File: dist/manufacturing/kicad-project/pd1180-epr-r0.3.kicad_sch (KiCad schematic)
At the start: 0 parts

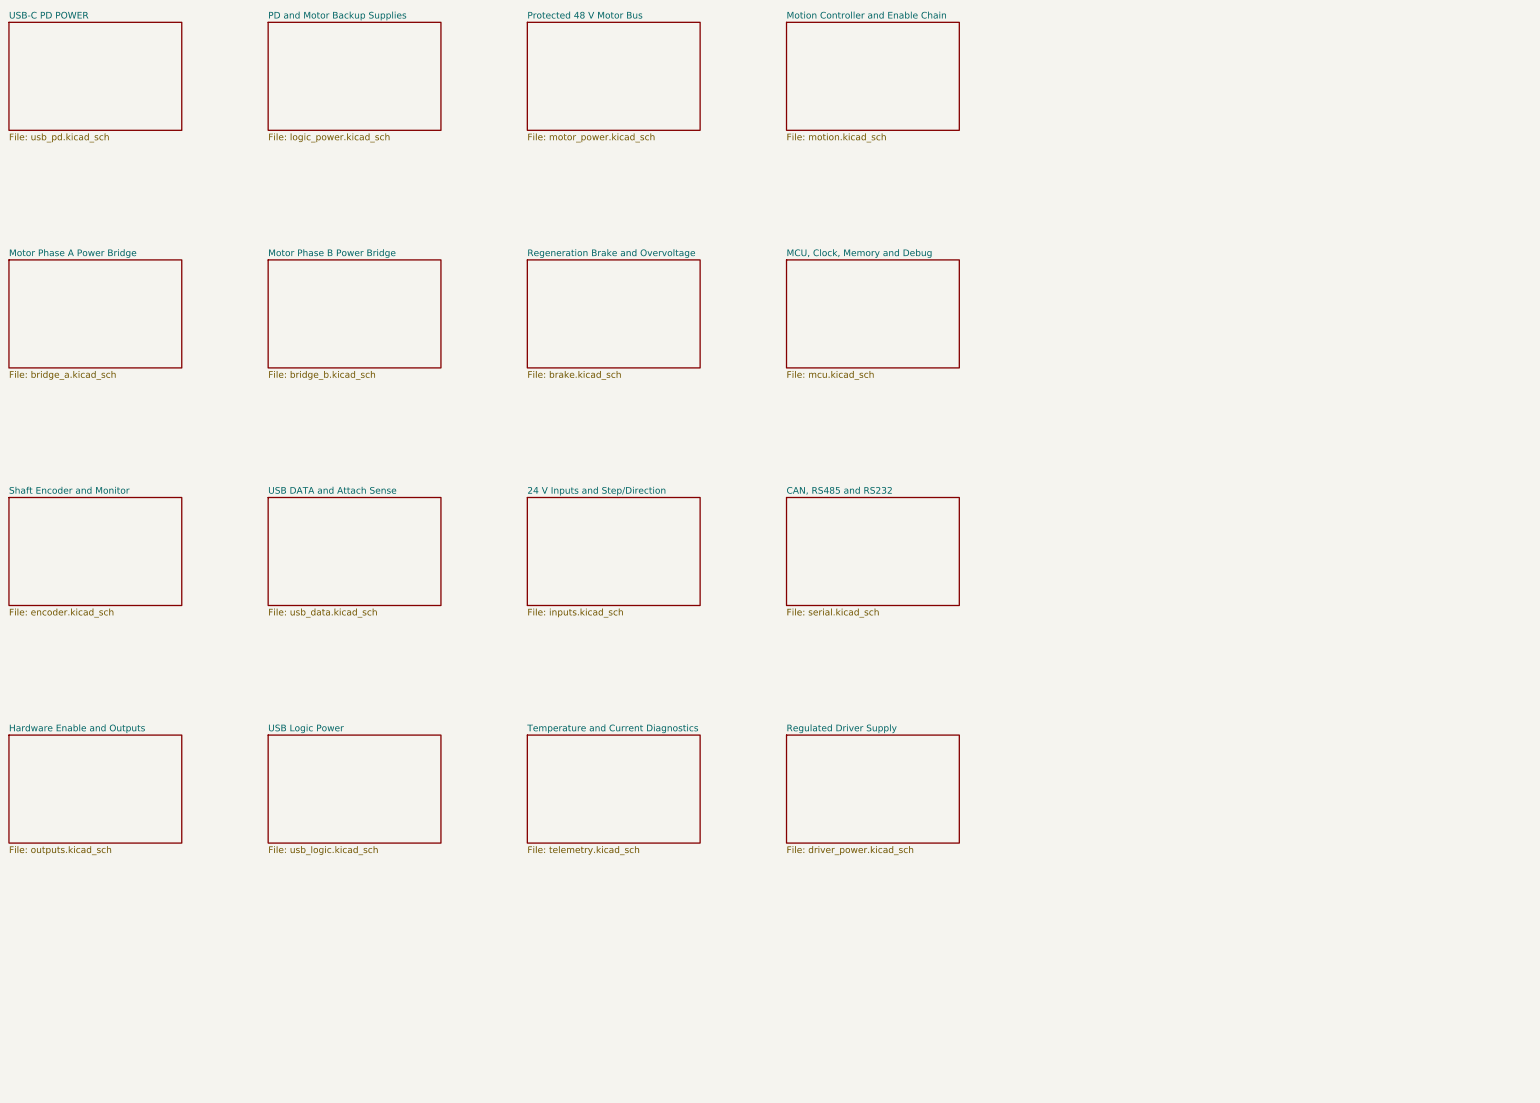
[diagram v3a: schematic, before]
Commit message: Add routed diagnostics and isolated PD programming access
Add RGB and independent power indication, a reset-safe driven buzzer,
isolated EEPROM programming access, and eight power/programming probes.
Preserve top-side assembly and local bypass paths, and exclude all bare
service contacts from stencil paste.

Refresh firmware, Gerbers, BOM/CPL, 3D models and review documentation.
The full review passes 32 checks and 55 regression tests, with zero native
DRC, ERC, unconnected and schematic-parity issues. TI configuration and
physical qualification remain explicit order holds.
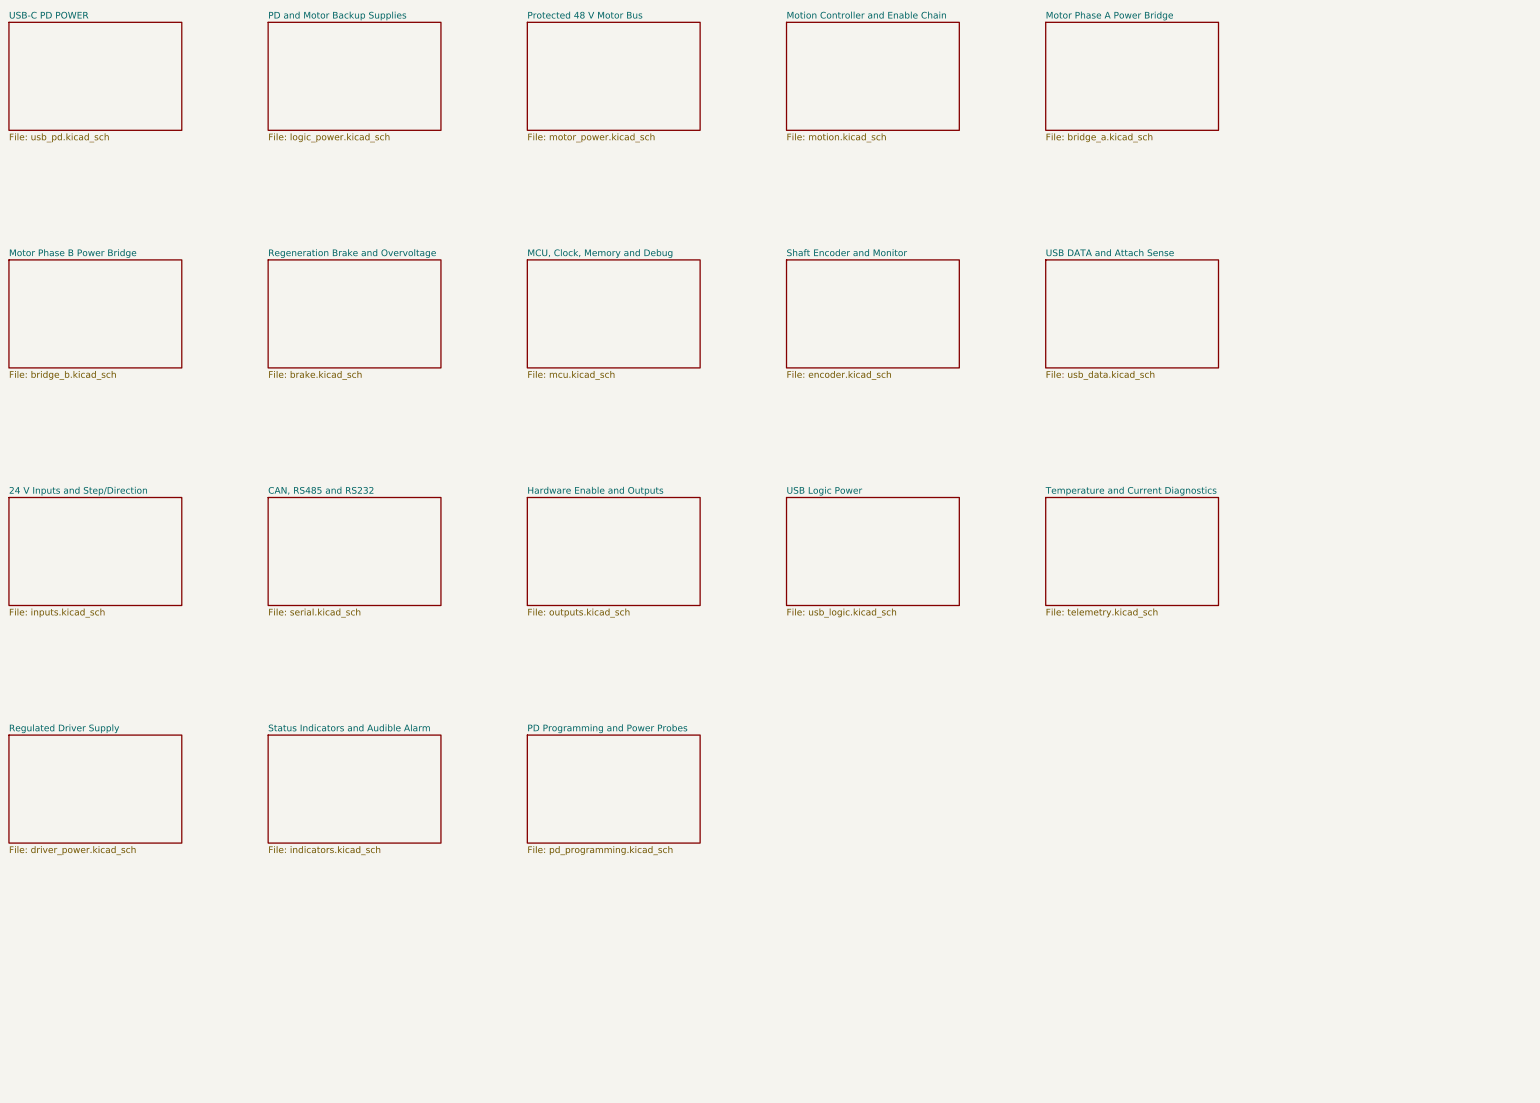
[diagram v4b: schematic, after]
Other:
- added sheet PD Programming and Power Probes (pd_programming.kicad_sch)
- added sheet Status Indicators and Audible Alarm (indicators.kicad_sch)

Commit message: Fix source warnings and organize schematic on A4 sheets
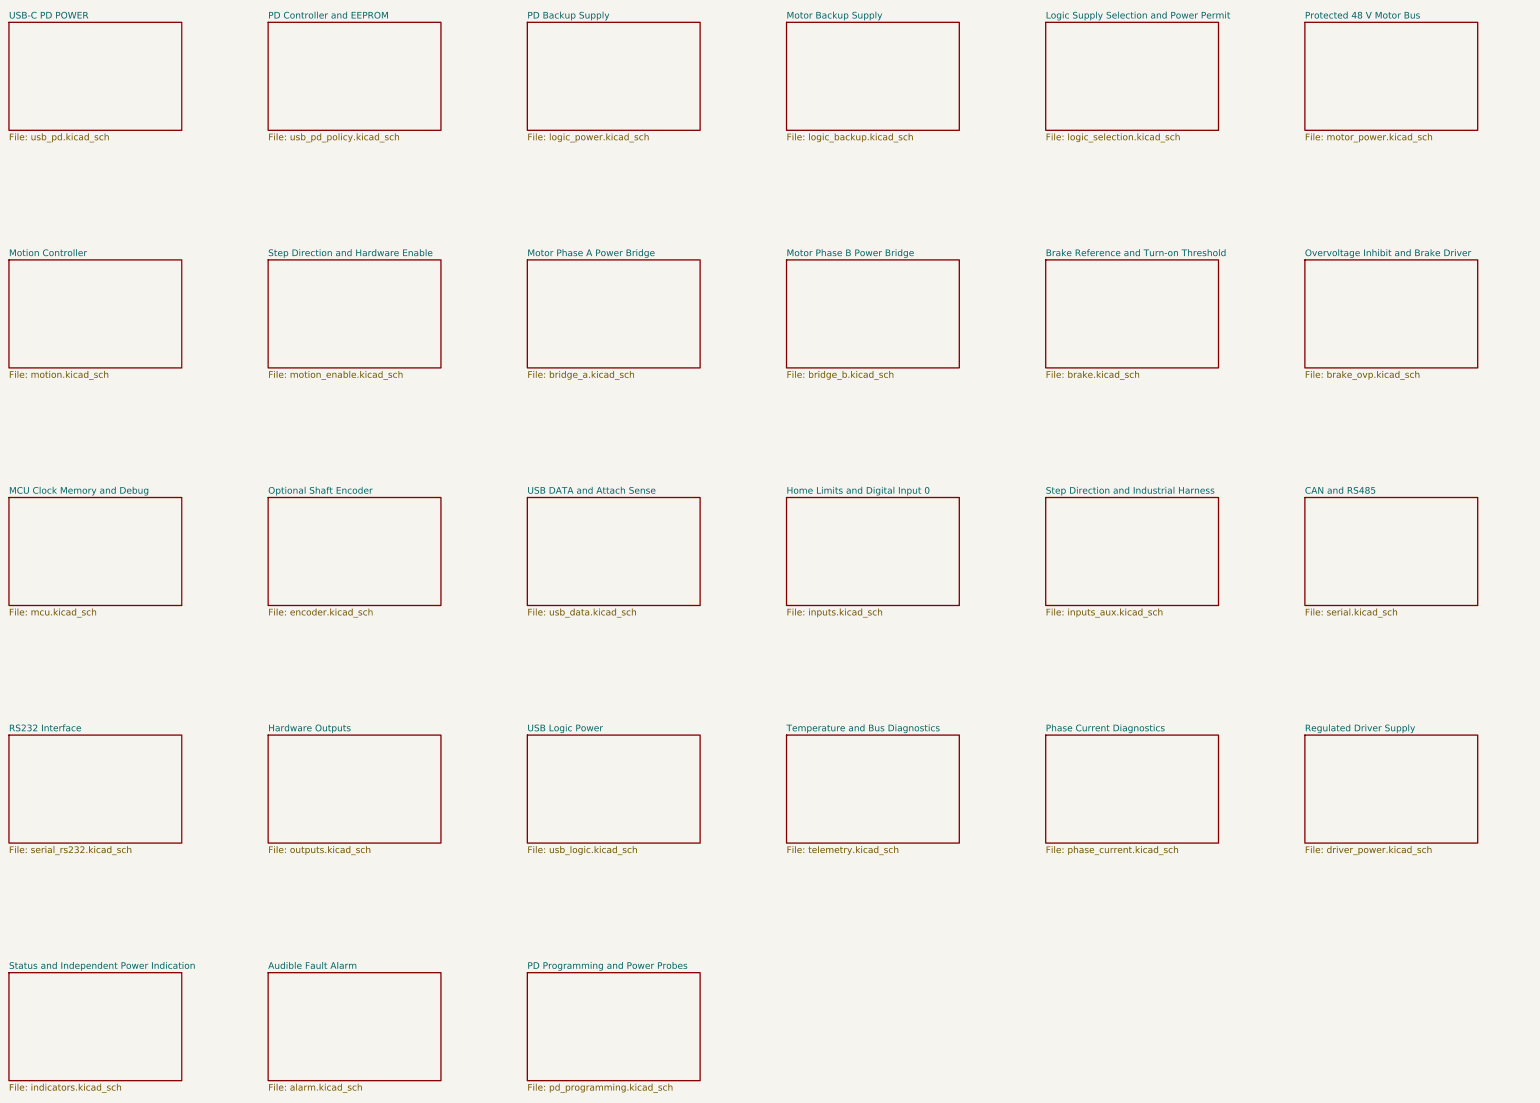
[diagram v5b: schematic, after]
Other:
- removed sheet 24 V Inputs and Step/Direction
- removed sheet CAN, RS485 and RS232
- removed sheet Hardware Enable and Outputs
- removed sheet MCU, Clock, Memory and Debug
- removed sheet Motion Controller and Enable Chain
- removed sheet PD and Motor Backup Supplies
- removed sheet Regeneration Brake and Overvoltage
- removed sheet Shaft Encoder and Monitor
- removed sheet Status Indicators and Audible Alarm
- removed sheet Temperature and Current Diagnostics
- added sheet Audible Fault Alarm (alarm.kicad_sch)
- added sheet Brake Reference and Turn-on Threshold (brake.kicad_sch)
- added sheet CAN and RS485 (serial.kicad_sch)
- added sheet Hardware Outputs (outputs.kicad_sch)
- added sheet Home Limits and Digital Input 0 (inputs.kicad_sch)
- added sheet Logic Supply Selection and Power Permit (logic_selection.kicad_sch)
- added sheet MCU Clock Memory and Debug (mcu.kicad_sch)
- added sheet Motion Controller (motion.kicad_sch)
- added sheet Motor Backup Supply (logic_backup.kicad_sch)
- added sheet Optional Shaft Encoder (encoder.kicad_sch)
- added sheet Overvoltage Inhibit and Brake Driver (brake_ovp.kicad_sch)
- added sheet PD Backup Supply (logic_power.kicad_sch)
- added sheet PD Controller and EEPROM (usb_pd_policy.kicad_sch)
- added sheet Phase Current Diagnostics (phase_current.kicad_sch)
- added sheet RS232 Interface (serial_rs232.kicad_sch)
- added sheet Status and Independent Power Indication (indicators.kicad_sch)
- added sheet Step Direction and Hardware Enable (motion_enable.kicad_sch)
- added sheet Step Direction and Industrial Harness (inputs_aux.kicad_sch)
- added sheet Temperature and Bus Diagnostics (telemetry.kicad_sch)

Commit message: Implement motor harness and mounting; remove unsupported interfaces
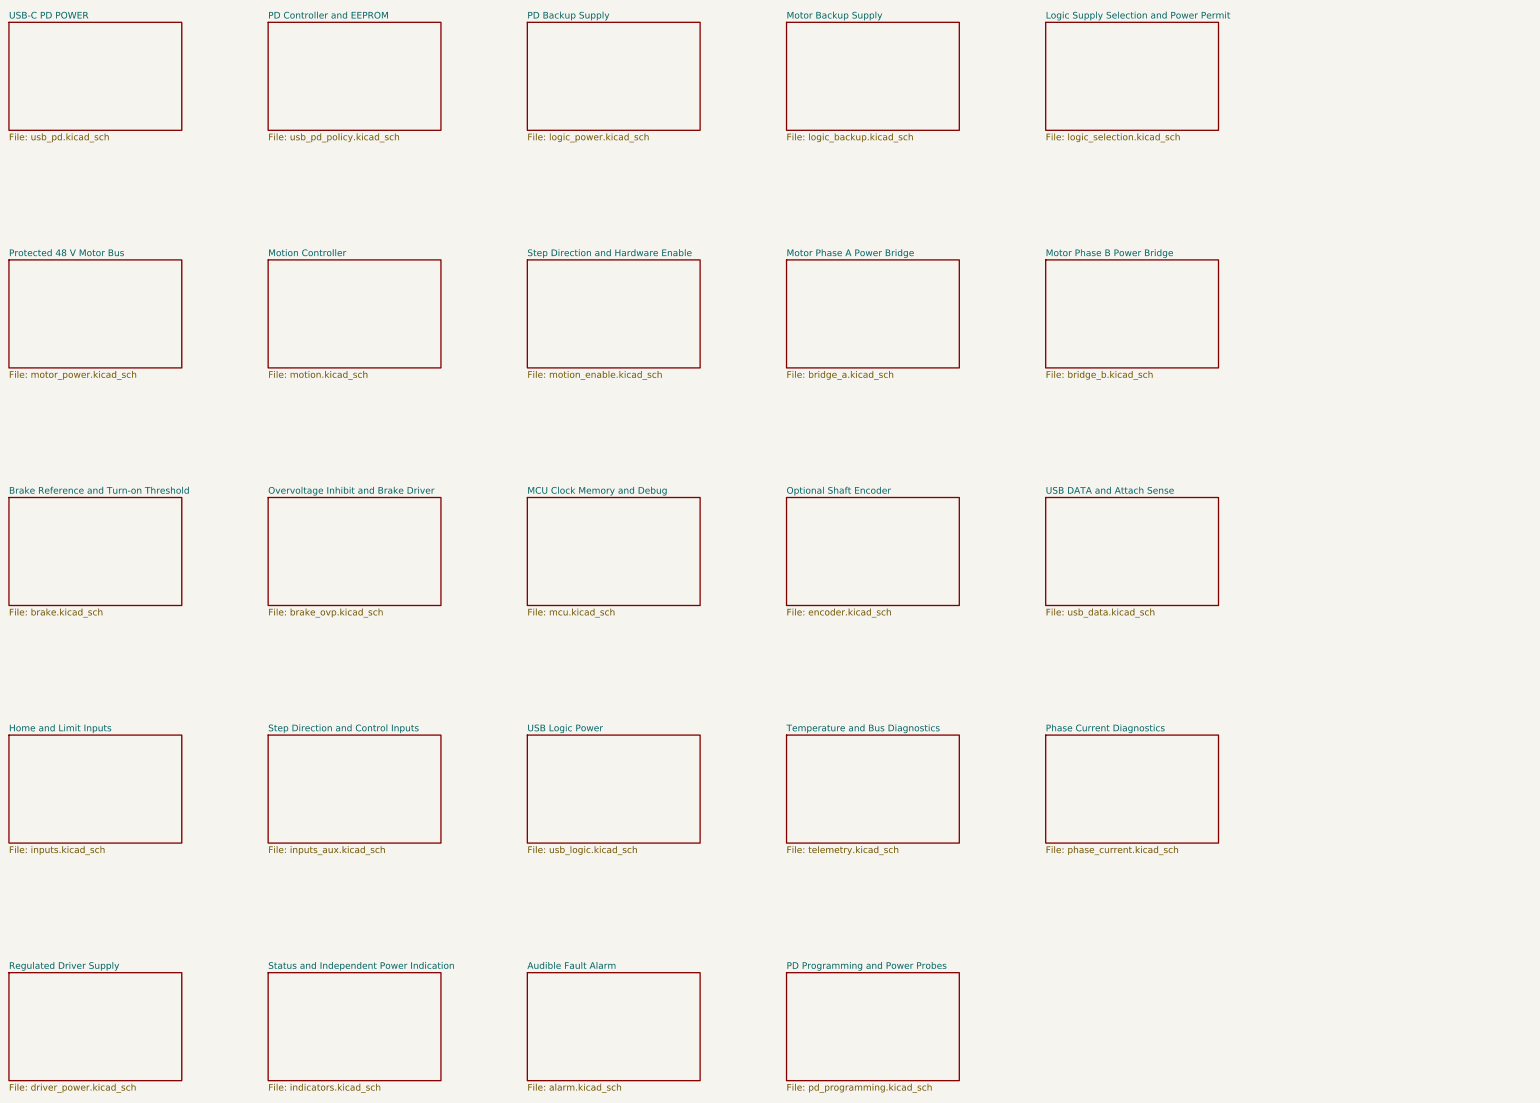
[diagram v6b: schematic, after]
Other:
- removed sheet CAN and RS485
- removed sheet Hardware Outputs
- removed sheet Home Limits and Digital Input 0
- removed sheet RS232 Interface
- removed sheet Step Direction and Industrial Harness
- added sheet Home and Limit Inputs (inputs.kicad_sch)
- added sheet Step Direction and Control Inputs (inputs_aux.kicad_sch)
